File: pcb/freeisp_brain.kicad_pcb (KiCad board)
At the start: 2 copper layers, 100 x 100 mm, 33 parts, among them J1 12V IN, J10 BUZZER, J11 HORN, J13 BOOST IN+ IN- OUT+ OUT-, J4 TFT, J5 RC522, J7 REED, J8 LED R, J9 LED G, K1 HORN RLY, U1 BUCK IN+ IN- OUT+ OUT-, U2 CHARGER IN+ IN- OUT+ OUT-, U3A ESP32 L, U3B ESP32 R, U4 MPU-6050

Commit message: Rev G: 115x115mm per Francis + devkit body keep-out on silk
His "11.5" was the board size - 11.5cm, so everything fits without
cramping around the 38-pin devkit's body overhang seen on the paper test.
Bottom row dropped to y=101 and the peripheral headers moved to x=97, so
the USB/Type-C overhang now has ~15mm of clear air before the first tall
part. The devkit's true body (with estimated 6mm antenna / 12mm USB
overhangs - verify on paper) is drawn on the silkscreen as an "ESP32 BODY
- LOW PARTS ONLY" box; only flat parts (discs, resistors) live inside it.

Row spacing: not yet measured, Francis delegated the call - staying at
25.4mm (DevKitC standard, consistent with his photo). The paper test
proves it before ordering either way.

Cost note, accepted: 115mm leaves PCBWay's 100mm tier (~$5 -> ~$15-25/5).
Flagged separately: the enclosure brain-module bay (FIR_ModulePlate
130x115 interior) no longer fits a 115x115 board - CAD rework needed.

All checks green: audit PASS, trace PASS, DRC 0 errors 0 unconnected.

Co-Authored-By: Claude Opus 5 (1M context) <noreply@anthropic.com>
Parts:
- moved H4 21.2 mm to (170.5, 150.5)
- moved H2 15.0 mm to (170.5, 44.5)
- moved H3 15.0 mm to (64.5, 150.5)
- moved J10 15.0 mm to (118.0, 141.0)
- moved J11 15.0 mm to (138.0, 141.0)
- moved J4 15.0 mm to (157.0, 52.0)
- moved J5 15.0 mm to (157.0, 76.0)
- moved J7 15.0 mm to (73.0, 141.0)
- moved J8 15.0 mm to (96.0, 141.0)
- moved J9 15.0 mm to (108.0, 141.0)
- moved K1 15.0 mm to (128.0, 141.0)
- moved U4 15.0 mm to (157.0, 100.0)
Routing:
- net GND: track 549.9 -> 624.9 mm
- net TFT_CS: track 109.5 -> 63.7 mm, vias 0 -> 2
- net +5V_SYS: track 192.3 -> 238.0 mm
- net TFT_DC: track 125.6 -> 82.6 mm
- net TFT_RST: track 114.1 -> 83.0 mm, vias 1 -> 0
- net REED_F: track 46.5 -> 66.5 mm, vias 1 -> 2
- net MOSI: track 95.4 -> 75.6 mm, vias 3 -> 0
- net +3V3: track 87.3 -> 103.3 mm, vias 1 -> 3
- net SCL: track 88.4 -> 103.4 mm
- net SDA: track 72.5 -> 87.5 mm
- net RC_SS: track 48.6 -> 63.6 mm
- net RC_RST: track 27.2 -> 42.2 mm
- net LED_G_A: track 23.4 -> 38.4 mm
- net HORN_DRV: track 10.6 -> 25.6 mm
- net LED_R_A: track 10.6 -> 25.6 mm
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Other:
- board size 100 x 100 mm -> 115 x 115 mm
- board text added: "ESP32 BODY - LOW PARTS ONLY"
- board text added: "FREEISP BRAIN REV G - 115MM - 38-PIN DEVKITC"
- board text removed: "FREEISP BRAIN REV F - 38-PIN DEVKITC"

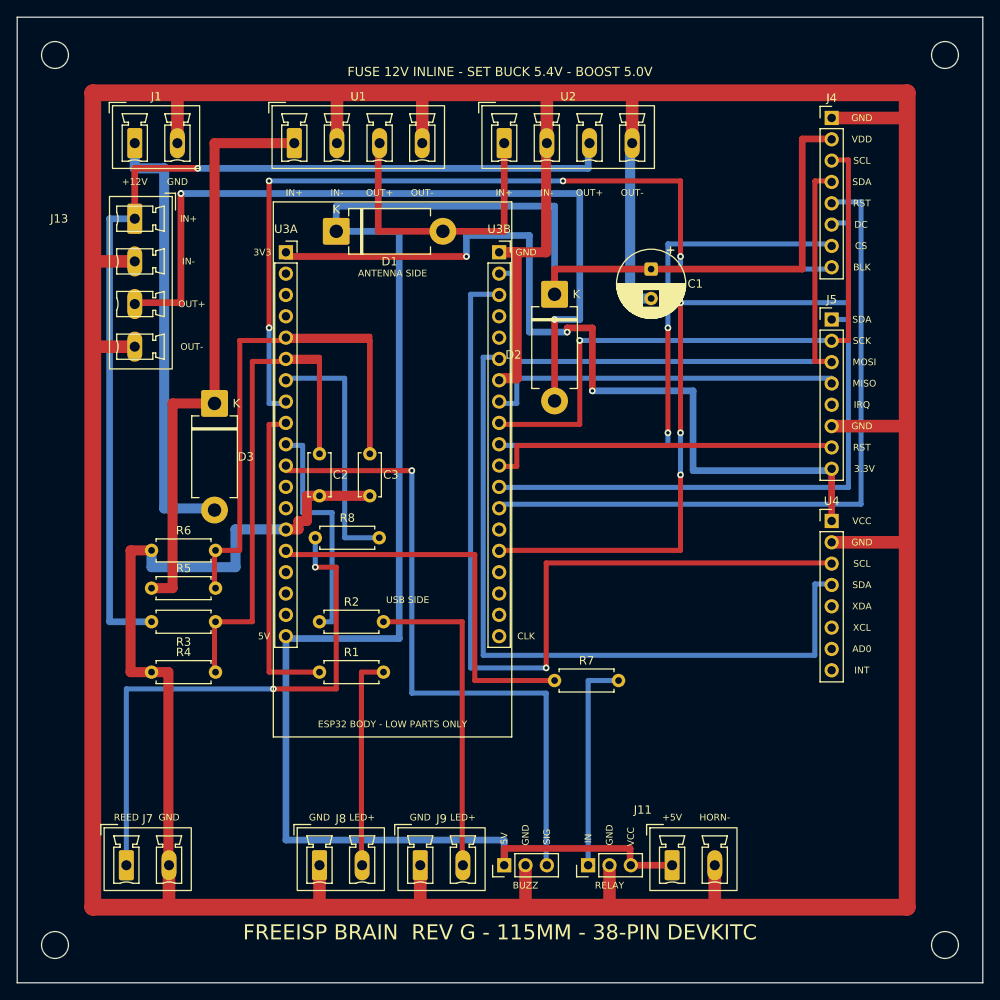
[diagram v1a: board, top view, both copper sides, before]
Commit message: Rev H: ESP32 keep-out emptied, block moved right into the free space
Francis's call, both parts of it:
- NOTHING under the devkit body. The keep-out box is now genuinely empty;
  C2/C3 moved beside their own dividers on the left, R8 next to the reed
  terminal it protects, R1/R2/R7 into a column on the right.
- The ESP32 block moved RIGHT (not left - he corrected me, the space is on
  the right) and down, so the board area is actually used.
- D1/D2/C1 regrouped as a power corner right of U3B.

Cost, accepted: 19 -> 25 vias, since traces now route around the keep-out
instead of under it. Vias are free at a fab; a resistor pressed against the
devkit's underside is not.

Router improvement that this needed: when a net fails to route, it is
promoted to the front of the queue and the whole strategy retried (up to 4
rounds). Two connections that failed after the parts moved were recovered
this way instead of by hand-nudging parts until the router got lucky.

All checks green: audit PASS, trace PASS (98 connections, 20 no-connects),
DRC 0 errors 0 unconnected. Board is 115x115mm, 38-pin DevKitC.

Co-Authored-By: Claude Opus 5 (1M context) <noreply@anthropic.com>
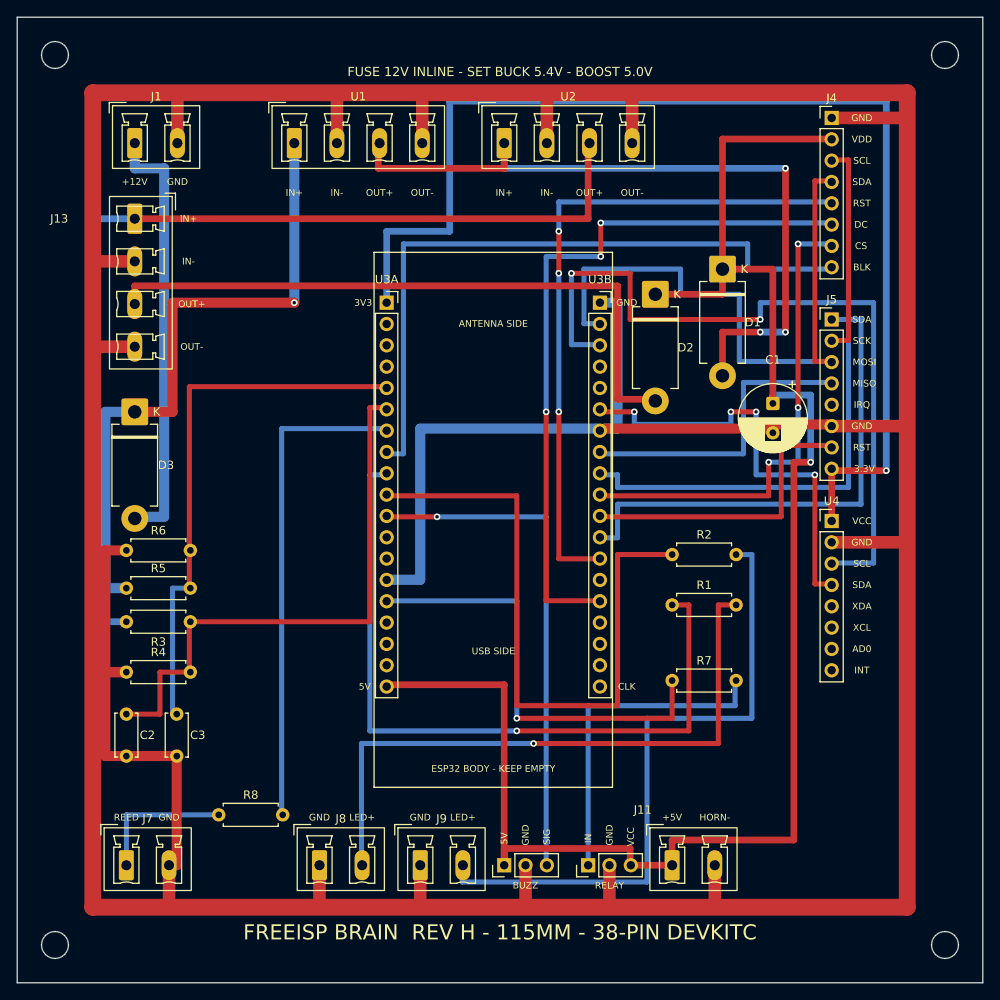
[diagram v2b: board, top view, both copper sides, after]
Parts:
- moved D1 46.2 mm to (144.0, 70.0), turned to 270 degrees
- moved R1 42.8 mm to (138.0, 110.0)
- moved R2 42.8 mm to (138.0, 104.0)
- moved C2 38.6 mm to (73.0, 123.0)
- moved C3 38.6 mm to (79.0, 123.0)
- moved R8 34.9 mm to (84.0, 135.0)
- moved C1 21.6 mm to (150.0, 86.0)
- moved R7 14.0 mm to (138.0, 119.0)
- moved U3A 13.4 mm to (104.0, 74.0)
- moved U3B 13.4 mm to (129.4, 74.0)
- moved D2 12.0 mm to (136.0, 73.0)
- moved D3 9.55 mm to (74.0, 87.0)
- moved R3 3.00 mm to (73.0, 112.0)
- moved R4 3.00 mm to (73.0, 118.0)
- moved R5 3.00 mm to (73.0, 108.0)
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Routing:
- net +5V: track 36.0 -> 89.7 mm, vias 0 -> 3
- net LED_R_A: track 25.6 -> 75.6 mm, vias 0 -> 1
- net LED_R: track 37.5 -> 87.5 mm, vias 0 -> 1
- net REED_F: track 66.5 -> 17.0 mm, vias 2 -> 0
- net LED_G: track 28.0 -> 77.0 mm
- net +5V_SYS: track 238.0 -> 199.0 mm, vias 0 -> 1
- net LED_G_A: track 38.4 -> 77.4 mm
- net +3V3: track 103.3 -> 140.3 mm, vias 3 -> 1
- net SDA: track 87.5 -> 51.3 mm, vias 0 -> 4
- net REED: track 30.2 -> 58.6 mm
- net TFT_BLK: track 106.1 -> 81.1 mm, vias 4 -> 0
- net SENSE_MAINS: track 85.4 -> 65.2 mm
- net BUZZ: track 78.6 -> 60.5 mm
- net +5V_BAT: track 93.7 -> 77.7 mm, vias 2 -> 0
- net HORN_DRV: track 25.6 -> 39.5 mm
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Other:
- board text added: "ESP32 BODY - KEEP EMPTY"
- board text added: "FREEISP BRAIN REV H - 115MM - 38-PIN DEVKITC"
- board text removed: "ESP32 BODY - LOW PARTS ONLY"
- board text removed: "FREEISP BRAIN REV G - 115MM - 38-PIN DEVKITC"
